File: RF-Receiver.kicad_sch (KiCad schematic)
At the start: 25 parts, among them J1 U.FL-R-SMT_01_, SW1 Button, U1 ESP32-PICO-D4, U2 SX1280IMLTRT, U3 LDO, Y1 Crystal

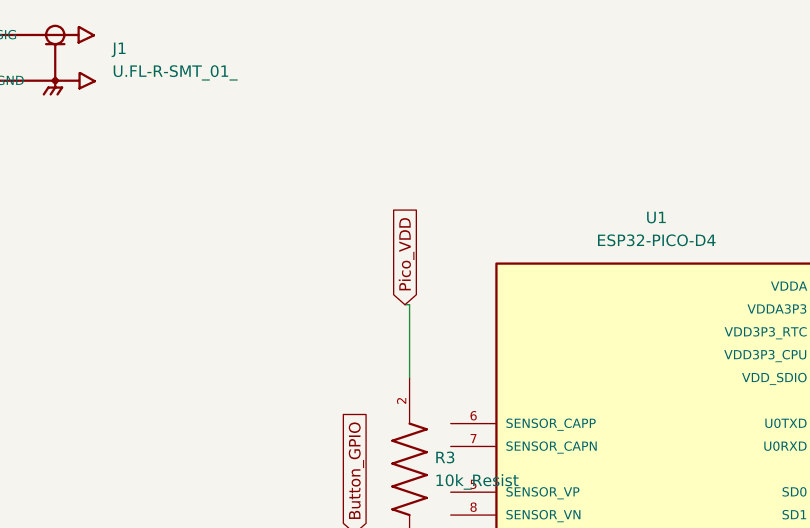
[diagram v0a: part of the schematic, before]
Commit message: Project Files
Update to board and schematic
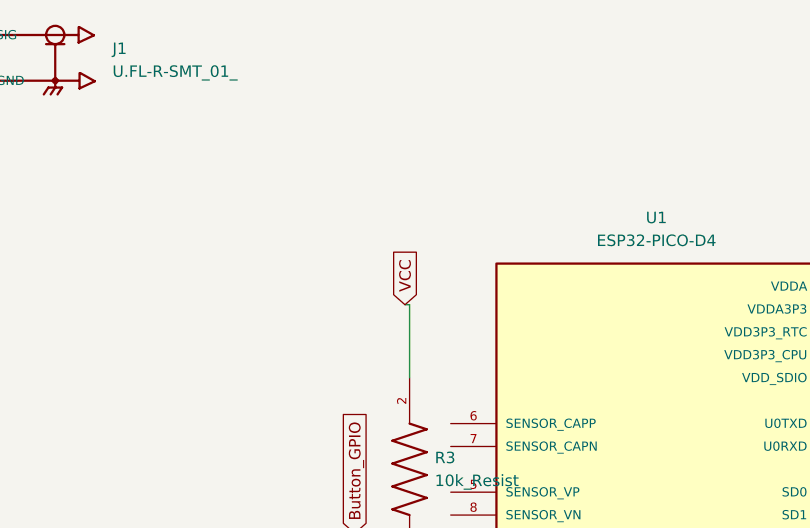
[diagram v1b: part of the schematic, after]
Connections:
- net Pico_VDD: no longer R3.2
- net VCC: now also R3.2
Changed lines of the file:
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@@
+		)
+	)
+	(global_label "VCC"
+		(shape input)
+		(at 104.14 51.562 90)
+		(fields_autoplaced yes)
+		(effects
+			(font
+				(size 1.27 1.27)
+			)
+			(justify left)
+		)
+		(property "Intersheetrefs" "VCC"
+			(at 104.14 44.9482 90)
+			(effects
+				(font
+					(size 1.27 1.27)
+				)
+				(justify left)
+				(hide yes)
+			)
 		)
 	)
@@
 				(hide yes)
 			)
-		)
-	)
-	(global_label "Pico_VDD"
-		(shape input)
-		(at 104.14 51.562 90)
-		(fields_autoplaced yes)
-		(effects
-			(font
-				(size 1.27 1.27)
-			)
-			(justify left)
-		)
-		(property "Intersheetrefs" "Pico_VDD"
-			(at 104.14 39.8682 90)
-			(effects
-				(font
-					(size 1.27 1.27)
-				)
-				(justify left)
-				(hide yes)
-			)
